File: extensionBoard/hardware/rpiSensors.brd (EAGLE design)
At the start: 100 x 80 mm, 31 parts, among them IC1 MEGA8-P

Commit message: minor
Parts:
- added C2, C4: (no value), capacitor-wima:C5B2.5
- added Q1: (no value), crystal:HC49/S
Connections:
- removed net +5V: C3.2, IC1.20, IC1.7, SV1.2, X1.2, X2.2, X3.2, X4.2, X5.2, X6.2
- new net +3V3: C3.2, IC1.7, SV1.1, X1.2, X2.2, X3.2, X4.2, X5.2, X6.2
- new net AVCC: IC1.20
- new net N$37: C2.2, IC1.9, Q1.2
- new net N$38: C4.2, IC1.10, Q1.1
- net GND: now also C2.1, C4.1
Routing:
- net +5V: track 200.5 -> 0.00 mm
- net +3V3: track 0.00 -> 190.0 mm
- net N$1: track 47.4 -> 91.7 mm
- net N$3: track 96.0 -> 67.1 mm, vias 0 -> 1
- net GND: track 21.6 -> 0.00 mm, vias 6 -> 0
- net N$2: track 42.4 -> 38.7 mm
- net N$6: track 53.7 -> 55.4 mm
- net N$7: track 48.7 -> 46.9 mm

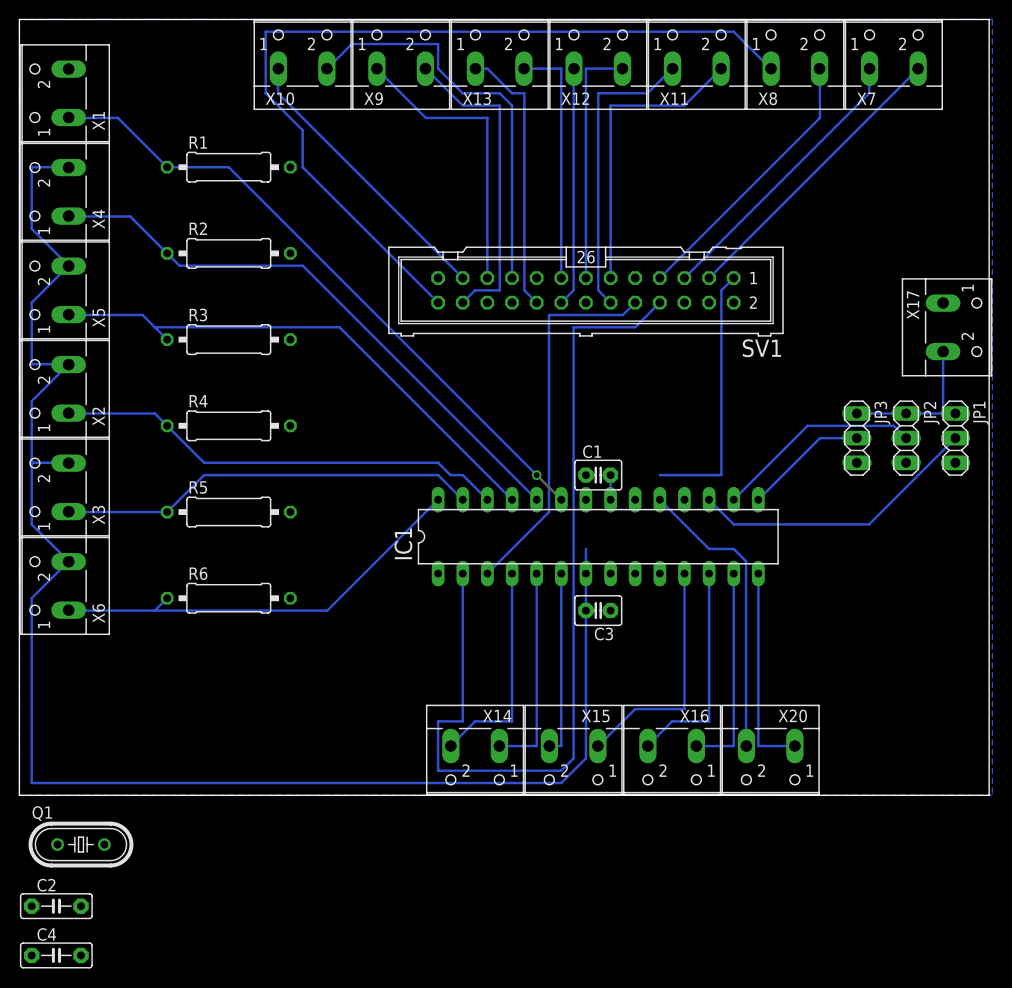
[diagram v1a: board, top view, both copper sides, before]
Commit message: revived schematics
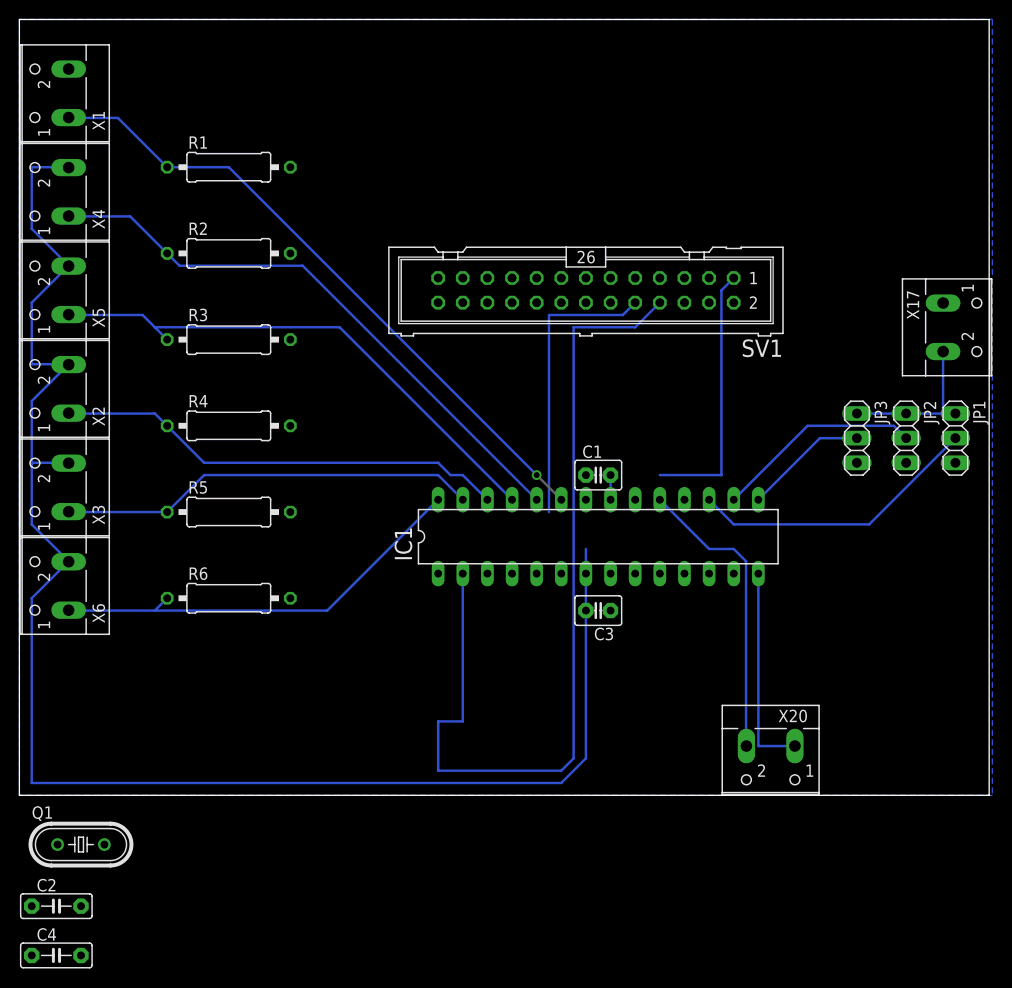
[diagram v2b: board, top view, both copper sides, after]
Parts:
- removed X10, X11, X12, X13, X14, X15, X16, X7, X8, X9: (no value), con-wago-500:W237-102
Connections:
- removed net N$10: SV1.5, X7.1
- removed net N$11: SV1.7, X8.2
- removed net N$12: SV1.26, X8.1
- removed net N$13: SV1.24, X9.2
- removed net N$14: SV1.21, X9.1
- removed net N$15: SV1.19, X10.2
- removed net N$16: SV1.23, X10.1
- removed net N$17: SV1.11, X11.2
- removed net N$18: SV1.12, X11.1
- removed net N$19: SV1.13, X12.2
- removed net N$20: SV1.15, X13.2
- removed net N$21: SV1.16, X12.1
- removed net N$22: SV1.18, X13.1
- removed net N$29: IC1.4, X14.2
- removed net N$30: IC1.5, X14.1
- removed net N$31: IC1.6, X15.2
- removed net N$32: IC1.11, X15.1
- removed net N$33: IC1.12, X16.2
- removed net N$34: IC1.13, X16.1
- removed net N$9: SV1.3, X7.2
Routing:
- net N$12: track 89.0 -> 0.00 mm
- net N$15: track 42.0 -> 0.00 mm
- net N$13: track 32.6 -> 0.00 mm
- net N$17: track 30.8 -> 0.00 mm
- net N$18: track 30.8 -> 0.00 mm
- net N$9: track 30.6 -> 0.00 mm
- net N$14: track 30.1 -> 0.00 mm
- net N$10: track 29.5 -> 0.00 mm
- net N$16: track 29.5 -> 0.00 mm
- net N$11: track 28.5 -> 0.00 mm
- net N$22: track 28.2 -> 0.00 mm
- net N$20: track 25.4 -> 0.00 mm
- net N$19: track 25.4 -> 0.00 mm
- net N$21: track 24.7 -> 0.00 mm
- net N$32: track 24.5 -> 0.00 mm
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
